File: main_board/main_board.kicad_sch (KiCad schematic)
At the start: 9 parts, among them J1 Bus_ISA_8bit, J2 IDE_44pin, J3 SIMM_30pin, J4 Keyboard, J5 Mouse, J6 5V_in, U1 M6117D, U2 SST39SF040

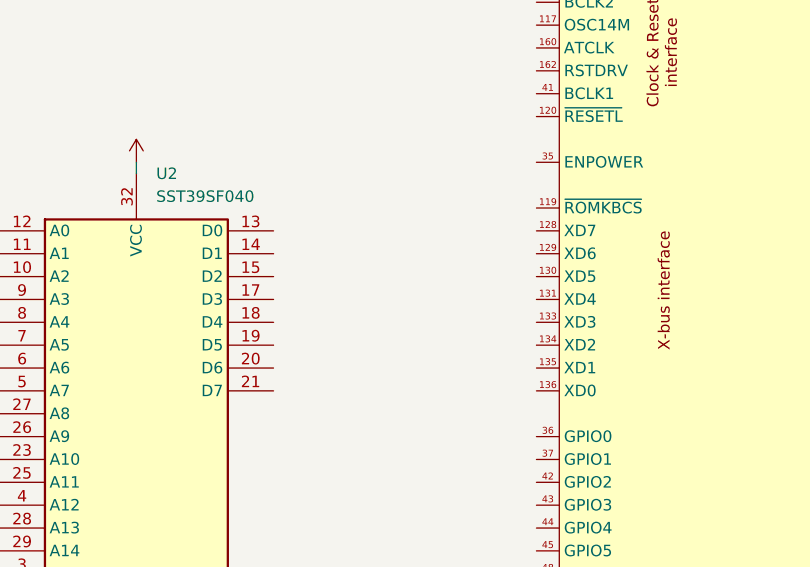
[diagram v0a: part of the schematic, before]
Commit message: connect CMOS flash to X-bus
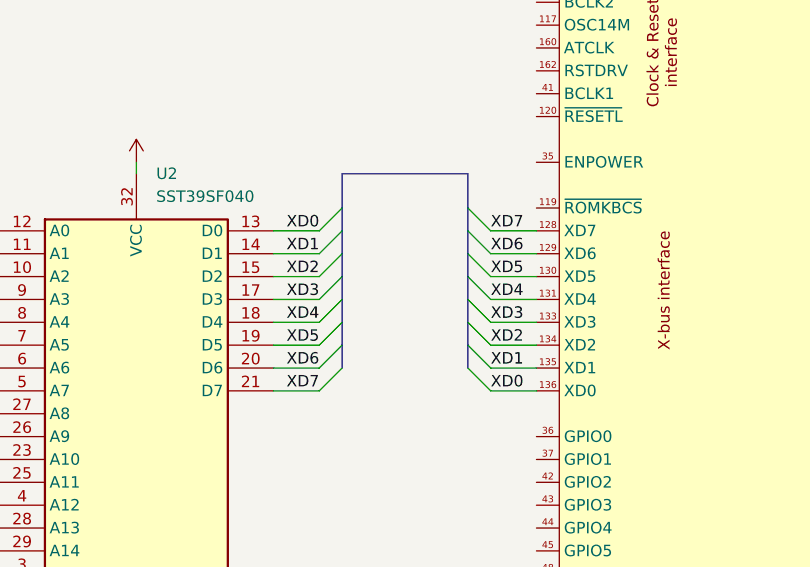
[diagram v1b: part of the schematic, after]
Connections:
- net XD0: now reaches U2.13 (D0)
- net XD0: now also U1.136 (XD0)
- net XD1: now reaches U2.14 (D1)
- net XD1: now also U1.135 (XD1)
- net XD2: now reaches U2.15 (D2)
- net XD2: now also U1.134 (XD2)
- net XD3: now reaches U2.17 (D3)
- net XD3: now also U1.133 (XD3)
- net XD4: now reaches U2.18 (D4)
- net XD4: now also U1.131 (XD4)
- net XD5: now reaches U2.19 (D5)
- net XD5: now also U1.130 (XD5)
- net XD6: now reaches U2.20 (D6)
- net XD6: now also U1.129 (XD6)
- net XD7: now reaches U2.21 (D7)
- net XD7: now also U1.128 (XD7)

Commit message: replace 8 bit ISA with 16 bit
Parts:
- removed J1: Bus_ISA_8bit, symbol Connector:Bus_ISA_8bit
- added J1: Bus_ISA_16bit, symbol Connector:Bus_ISA_16bit
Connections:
- net +5V: now also J1.29 (VCC), J1.3 (+5V)
- net AEN: now also J1.42 (AEN)
- net ALE: now also J1.28 (ALE)
- net DA0: now also J1.19 (~{REFRESH})
- net DA1: now also J1.17 (~{DACK1})
- net DA2: now also J1.26 (~{DACK2})
- net DA3: now also J1.15 (~{DACK3})
- net DRQ1: now also J1.18 (DRQ1)
- net DRQ2: now also J1.6 (DRQ2)
- net DRQ3: now also J1.16 (DRQ3)
- net GND: now also J1.1 (GND), J1.10 (GND), J1.31 (GND)
- net IOCH: now also J1.32 (IO)
- net IOR: now also J1.14 (~{IOR})
- net IORD: now also J1.41 (IO_READY)
- net IOW: now also J1.13 (~{IOW})
- net IRQ3: now also J1.25 (IRQ3)
- net IRQ4: now also J1.24 (IRQ4)
- net IRQ5: now also J1.23 (IRQ5)
- net IRQ6: now also J1.22 (IRQ6)
- net IRQ7: now also J1.21 (IRQ7)
- net IRQ9: now also J1.4 (IRQ2)
- net SA0: now also J1.62 (BA00)
- net SA1: now also J1.61 (BA01)
- net SA10: now also J1.52 (BA10)
- net SA11: now also J1.51 (BA11)
- net SA12: now also J1.50 (BA12)
- net SA13: now also J1.49 (BA13)
- net SA14: now also J1.48 (BA14)
- net SA15: now also J1.47 (BA15)
- net SA16: now also J1.46 (BA16)
- net SA17: now also J1.45 (BA17)
- net SA18: now also J1.44 (BA18)
- net SA19: now also J1.43 (BA19)
- net SA2: now also J1.60 (BA02)
- net SA3: now also J1.59 (BA03)
- net SA4: now also J1.58 (BA04)
- net SA5: now also J1.57 (BA05)
- net SA6: now also J1.56 (BA06)
- net SA7: now also J1.55 (BA07)
- net SA8: now also J1.54 (BA08)
- net SA9: now also J1.53 (BA09)
- net SD0: now also J1.40 (DB0)
- net SD1: now also J1.39 (DB1)
- net SD2: now also J1.38 (DB2)
- net SD3: now also J1.37 (DB3)
- net SD4: now also J1.36 (DB4)
- net SD5: now also J1.35 (DB5)
- net SD6: now also J1.34 (DB6)
- net SD7: now also J1.33 (DB7)
- net SMR: now also J1.12 (~{SMEMR})
- net SMW: now also J1.11 (~{SMEMW})
- net TC: now also J1.27 (TC)
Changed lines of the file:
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@@
-	)
-	(symbol
-		(lib_id "Connector:Bus_ISA_8bit")
-		(at 208.28 85.09 0)
-		(unit 1)
-		(exclude_from_sim no)
-		(in_bom yes)
-		(on_board yes)
-		(dnp no)
-		(fields_autoplaced yes)
-		(property "Reference" "J1"
-			(at 208.28 39.37 0)
-			(effects
-				(font
-					(size 1.27 1.27)
-				)
-			)
-		)
-		(property "Value" "Bus_ISA_8bit"
-			(at 208.28 41.91 0)
-			(effects
-				(font
-					(size 1.27 1.27)
-				)
-			)
-		)
-		(property "Footprint" ""
-			(at 208.28 85.09 0)
-			(effects
-				(font
-					(size 1.27 1.27)
-				)
-				(hide yes)
-			)
-		)
-		(property "Datasheet" "https://en.wikipedia.org/wiki/Industry_Standard_Architecture"
-			(at 208.28 85.09 0)
-			(effects
-				(font
-					(size 1.27 1.27)
-				)
-				(hide yes)
-			)
-		)
-		(property "Description" "8-bit ISA-PC bus connector"
-			(at 208.28 85.09 0)
-			(effects
-				(font
-					(size 1.27 1.27)
-				)
-				(hide yes)
-			)
-		)
-		(pin "14"
-		)
-		(pin "20"
-		)
-		(pin "1"
-		)
-		(pin "2"
-		)
-		(pin "12"
-		)
-		(pin "30"
-		)
-		(pin "31"
-		)
-		(pin "32"
-		)
-		(pin "33"
-		)
-		(pin "34"
-		)
-		(pin "35"
-		)
-		(pin "36"
-		)
-		(pin "37"
-		)
-		(pin "38"
-		)
-		(pin "39"
-		)
-		(pin "4"
-		)
-		(pin "40"
-		)
-		(pin "41"
-		)
-		(pin "42"
-		)
-		(pin "43"
-		)
-		(pin "44"
-		)
-		(pin "45"
-		)
-		(pin "46"
-		)
-		(pin "47"
-		)
-		(pin "48"
-		)
-		(pin "49"
-		)
-		(pin "5"
-		)
-		(pin "50"
-		)
-		(pin "51"
-		)
-		(pin "52"
-		)
-		(pin "53"
-		)
-		(pin "54"
-		)
-		(pin "55"
-		)
-		(pin "56"
-		)
-		(pin "57"
-		)
-		(pin "58"
-		)
-		(pin "59"
-		)
-		(pin "6"
-		)
-		(pin "60"
-		)
-		(pin "61"
-		)
-		(pin "62"
-		)
-		(pin "7"
-		)
-		(pin "8"
-		)
-		(pin "9"
-		)
-		(pin "29"
-		)
-		(pin "3"
-		)
-		(pin "23"
-		)
-		(pin "24"
-		)
-		(pin "21"
-		)
-		(pin "22"
-		)
-		(pin "25"
-		)
-		(pin "26"
-		)
-		(pin "13"
-		)
-		(pin "10"
-		)
-		(pin "16"
-		)
-		(pin "15"
-		)
-		(pin "11"
-		)
-		(pin "27"
-		)
-		(pin "28"
-		)
-		(pin "19"
-		)
-		(pin "17"
-		)
-		(pin "18"
-		)
-		(instances
-			(project "main_board"
-				(path "/7979ed65-ccda-4bb8-8907-913d5800ff08"
-					(reference "J1")
-					(unit 1)
-				)
-			)
-		)
 	)
 	(symbol
@@
 					(unit 1)
 				)
+			)
+		)
+	)
+	(symbol
+		(lib_id "Connector:Bus_ISA_16bit")
+		(at 208.28 110.49 0)
+		(unit 1)
+		(exclude_from_sim no)
+		(in_bom yes)
+		(on_board yes)
+		(dnp no)
+		(fields_autoplaced yes)
+		(property "Reference" "J1"
+			(at 208.28 39.37 0)
+			(effects
+				(font
+					(size 1.27 1.27)
+				)
+			)
+		)
+		(property "Value" "Bus_ISA_16bit"
+			(at 208.28 41.91 0)
+			(effects
+				(font
+					(size 1.27 1.27)
+				)
+			)
+		)
+		(property "Footprint" ""
+			(at 208.28 109.22 0)
+			(effects
+				(font
+					(size 1.27 1.27)
+				)
+				(hide yes)
+			)
+		)
+		(property "Datasheet" "https://en.wikipedia.org/wiki/Industry_Standard_Architecture"
+			(at 208.28 109.22 0)
+			(effects
+				(font
+					(size 1.27 1.27)
+				)
+				(hide yes)
+			)
+		)
+		(property "Description" "16-bit ISA-AT bus connector"
+			(at 208.28 110.49 0)
+			(effects
+				(font
+					(size 1.27 1.27)
+				)
+				(hide yes)
+			)
+		)
+		(pin "17"
+		)
+		(pin "18"
+		)
+		(pin "19"
+		)
+		(pin "2"
+		)
+		(pin "20"
+		)
+		(pin "21"
+		)
+		(pin "22"
+		)
+		(pin "23"
+		)
+		(pin "24"
+		)
+		(pin "25"
+		)
+		(pin "26"
+		)
+		(pin "27"
+		)
+		(pin "28"
+		)
+		(pin "29"
+		)
+		(pin "3"
+		)
+		(pin "30"
+		)
+		(pin "31"
+		)
+		(pin "32"
+		)
+		(pin "33"
+		)
+		(pin "34"
+		)
+		(pin "35"
+		)
+		(pin "36"
+		)
+		(pin "37"
+		)
+		(pin "38"
+		)
+		(pin "39"
+		)
+		(pin "69"
+		)
+		(pin "4"
+		)
+		(pin "40"
+		)
+		(pin "41"
+		)
+		(pin "42"
+		)
+		(pin "43"
+		)
+		(pin "44"
+		)
+		(pin "45"
+		)
+		(pin "46"
+		)
+		(pin "47"
+		)
+		(pin "48"
+		)
+		(pin "49"
+		)
+		(pin "5"
+		)
+		(pin "50"
+		)
+		(pin "51"
+		)
+		(pin "52"
+		)
+		(pin "53"
+		)
+		(pin "54"
+		)
+		(pin "55"
+		)
+		(pin "56"
+		)
+		(pin "57"
+		)
+		(pin "58"
+		)
+		(pin "59"
+		)
+		(pin "6"
+		)
+		(pin "60"
+		)
+		(pin "61"
+		)
+		(pin "62"
+		)
+		(pin "63"
+		)
+		(pin "64"
+		)
+		(pin "65"
+		)
+		(pin "66"
+		)
+		(pin "67"
+		)
+		(pin "68"
+		)
+		(pin "7"
+		)
+		(pin "70"
+		)
+		(pin "71"
+		)
+		(pin "72"
+		)
+		(pin "73"
+		)
+		(pin "74"
+		)
+		(pin "75"
+		)
+		(pin "76"
+		)
+		(pin "77"
+		)
+		(pin "78"
+		)
+		(pin "79"
+		)
+		(pin "8"
+		)
+		(pin "80"
+		)
+		(pin "81"
+		)
+		(pin "82"
+		)
+		(pin "83"
+		)
+		(pin "84"
+		)
+		(pin "85"
+		)
+		(pin "86"
+		)
+		(pin "87"
+		)
+		(pin "88"
+		)
+		(pin "89"
+		)
+		(pin "9"
+		)
+		(pin "90"
+		)
+		(pin "91"
+		)
+		(pin "92"
+		)
+		(pin "93"
+		)
+		(pin "94"
+		)
+		(pin "95"
+		)
+		(pin "96"
+		)
+		(pin "97"
+		)
+		(pin "98"
+		)
+		(pin "11"
+		)
+		(pin "12"
+		)
+		(pin "13"
+		)
+		(pin "14"
+		)
+		(pin "15"
+		)
+		(pin "16"
+		)
+		(pin "1"
+		)
+		(pin "10"
+		)
+		(instances
+			(project "main_board"
+				(path "/7979ed65-ccda-4bb8-8907-913d5800ff08"
+					(reference "J1")
+					(unit 1)
+				)

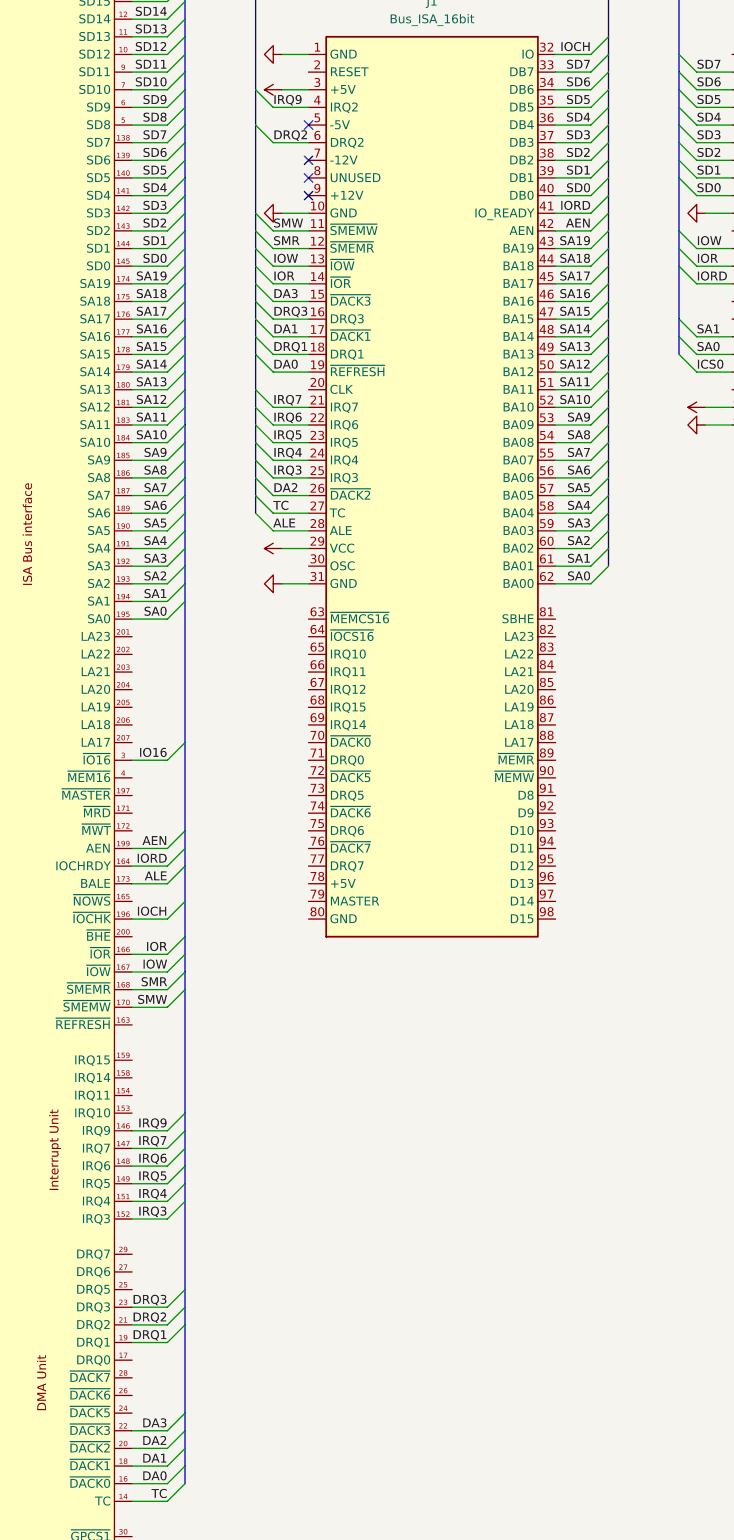
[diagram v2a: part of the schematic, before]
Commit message: connect additional signals to 16 bit bus
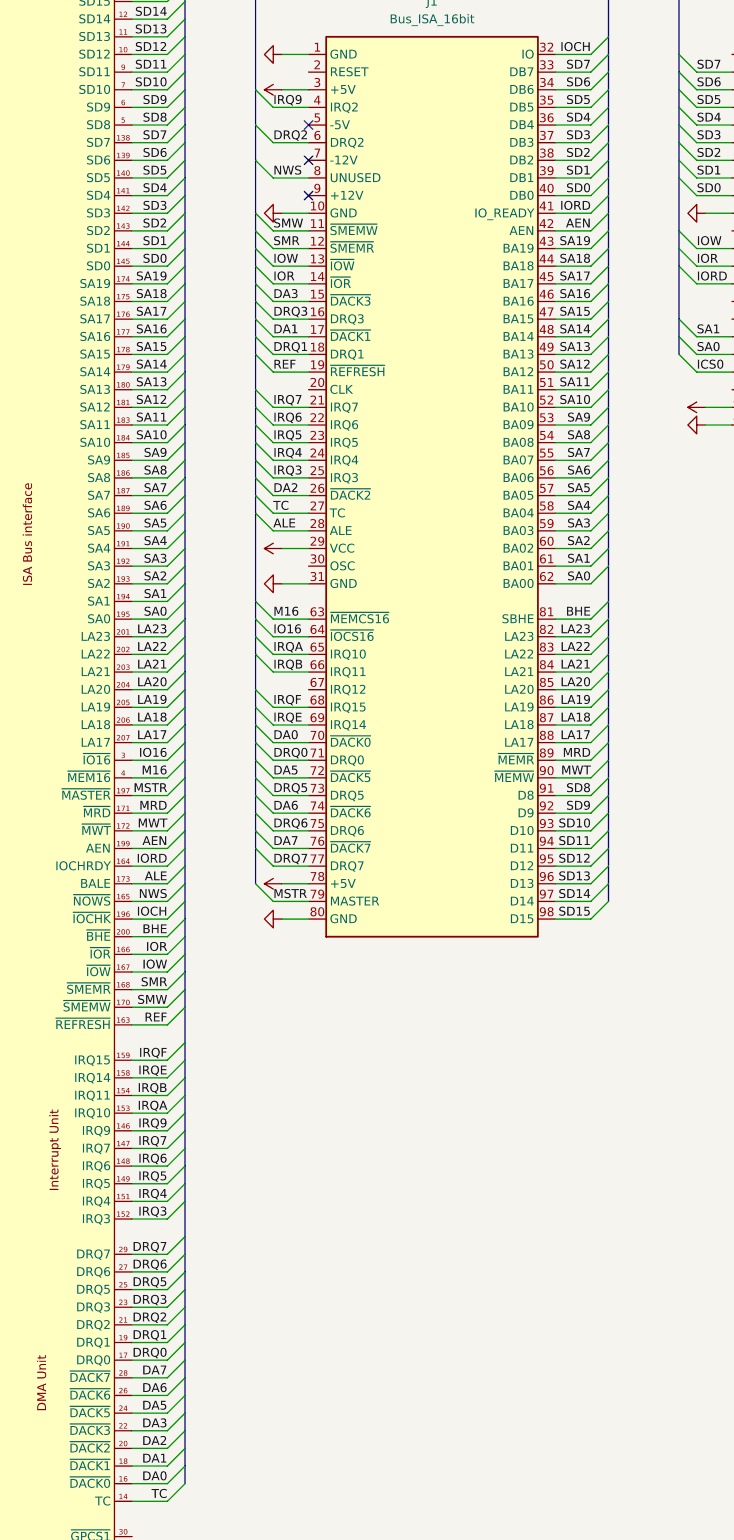
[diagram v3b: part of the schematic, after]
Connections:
- net +5V: now also J1.78 (+5V)
- net DA0: now also J1.70 (~{DACK0}); no longer J1.19 (~{REFRESH})
- net GND: now also J1.80 (GND)
- net IO16: now also J1.64 (~{IOCS16})
- net SD10: now also J1.93 (D10)
- net SD11: now also J1.94 (D11)
- net SD12: now also J1.95 (D12)
- net SD13: now also J1.96 (D13)
- net SD14: now also J1.97 (D14)
- net SD15: now also J1.98 (D15)
- net SD8: now also J1.91 (D8)
- net SD9: now also J1.92 (D9)
- net M16: now reaches J1.63 (~{MEMCS16})
- net M16: now also U1.4 (~{MEM16})
- net IRQA: now reaches J1.65 (IRQ10)
- net IRQA: now also U1.153 (IRQ10)
- net IRQB: now reaches J1.66 (IRQ11)
- net IRQB: now also U1.154 (IRQ11)
- net IRQF: now reaches J1.68 (IRQ15)
- net IRQF: now also U1.159 (IRQ15)
- net IRQE: now reaches J1.69 (IRQ14)
- net IRQE: now also U1.158 (IRQ14)
- net DRQ0: now reaches J1.71 (DRQ0)
- net DRQ0: now also U1.17 (DRQ0)
- net DA5: now reaches J1.72 (~{DACK5})
- net DA5: now also U1.24 (~{DACK5})
- net DRQ5: now reaches J1.73 (DRQ5)
- net DRQ5: now also U1.25 (DRQ5)
- net DA6: now reaches J1.74 (~{DACK6})
- net DA6: now also U1.26 (~{DACK6})
- net DRQ6: now reaches J1.75 (DRQ6)
- net DRQ6: now also U1.27 (DRQ6)
- net DA7: now reaches J1.76 (~{DACK7})
- net DA7: now also U1.28 (~{DACK7})
- net DRQ7: now reaches J1.77 (DRQ7)
- net DRQ7: now also U1.29 (DRQ7)
- net MSTR: now reaches J1.79 (MASTER)
- net MSTR: now also U1.197 (~{MASTER})
- net NWS: now reaches J1.8 (UNUSED)
- net NWS: now also U1.165 (~{NOWS})
- net BHE: now reaches J1.81 (SBHE)
- net BHE: now also U1.200 (~{BHE})
- net LA23: now reaches J1.82 (LA23)
- net LA23: now also U1.201 (LA23)
- net LA22: now reaches J1.83 (LA22)
- net LA22: now also U1.202 (LA22)
- net LA21: now reaches J1.84 (LA21)
- net LA21: now also U1.203 (LA21)
- net LA20: now reaches J1.85 (LA20)
- net LA20: now also U1.204 (LA20)
- net LA19: now reaches J1.86 (LA19)
- net LA19: now also U1.205 (LA19)
- net LA18: now reaches J1.87 (LA18)
- net LA18: now also U1.206 (LA18)
- net LA17: now reaches J1.88 (LA17)
- net LA17: now also U1.207 (LA17)
- net MRD: now reaches J1.89 (~{MEMR})
- net MRD: now also U1.171 (~{MRD})
- net MWT: now reaches J1.90 (~{MEMW})
- net MWT: now also U1.172 (~{MWT})
- net REF: now reaches U1.163 (~{REFRESH})
- net REF: now also J1.19 (~{REFRESH})
- no-connect marks 12 -> 11
